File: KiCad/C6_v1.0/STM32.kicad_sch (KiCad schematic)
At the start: 25 parts, among them J1 Conn_01x06_Pin, J2 Conn_01x06_Pin, U1 STM32H562RITx, U2 STM32H7A3RITx, U7 MAX3490xSA

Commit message: commit gng gng
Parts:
- added C32, C33: 2.2u, Capacitor_SMD:C_0805_2012Metric, symbol Device:C
- added J8, J9: Conn_01x02, symbol Connector_Generic:Conn_01x02
- added R49, R50: 10k, Resistor_SMD:R_0805_2012Metric, symbol Device:R
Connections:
- net 3V3: now also J8.1 (Pin_1), J9.1 (Pin_1)
- net GND: now also C32.2, C33.2, R49.2, R50.2
- net at U2.30 (VCAP): now also U2.46 (VCAP), C33.1
- net at U2.60 (BOOT0): now also J8.2 (Pin_2), R49.1
- net EGSE_TX: now reaches U1.16 (PA2)
- net EGSE_RX: now reaches U1.17 (PA3)
- net at U1.30 (VCAP): now also U1.62 (VCAP), C32.1
- net at U1.60 (BOOT0): now also J9.2 (Pin_2), R50.1

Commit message: made voltage sense more accurate to 1%
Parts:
- removed C3: 0.1u, Capacitor_SMD:C_0805_2012Metric, symbol Device:C
- removed FB1: FerriteBead, symbol Device:FerriteBead
- added U10: REF35330QDBVR, Package_TO_SOT_SMD:SOT-23-6, symbol Reference_Voltage:REF35330QDBVR
- C2: value 10u -> 1u
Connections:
- net 3V3: no longer C2.2
- net GND: now also U10.1 (GND), U10.2 (GND)
- net 3V3_REF: now reaches U1.13 (VDDA)
- net 3V3_REF: now also U10.6 (VREF)
- net Vsns: now reaches U1.26 (PB0)
- net I_SCL: now reaches U1.58 (PB6)
- net I_SDA: now reaches U1.59 (PB7)
- new net: C2.2, U10.5 (NR)
- new net 5V: U10.3 (EN), U10.4 (VIN)

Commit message: gooning
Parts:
- J1, J2: footprint (none) -> Connector_PinHeader_2.54mm:PinHeader_1x06_P2.54mm_Vertical

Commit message: gooning
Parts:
- J8, J9: footprint (none) -> Connector_PinHeader_2.54mm:PinHeader_1x02_P2.54mm_Vertical

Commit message: im scared
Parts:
- FB2: footprint (none) -> Resistor_SMD:R_0805_2012Metric

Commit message: DCMI1-Me0
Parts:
- C1, C2, C32, C33, C4, C5, C6, C9: footprint Capacitor_SMD:C_0805_2012Metric -> Capacitor_SMD:C_0402_1005Metric_Pad0.74x0.62mm_HandSolder
- R10, R11, R12, R13, R14, R15, R16, R23, R24, R49, R50, R8, R9: footprint Resistor_SMD:R_0805_2012Metric -> Resistor_SMD:R_0402_1005Metric_Pad0.72x0.64mm_HandSolder
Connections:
- net HALL_C: now reaches U1.20 (PA4)
- net HALL_B: now reaches U1.22 (PA6)
- net HALL_A: now reaches U1.23 (PA7)
- net ESC_PWM: now reaches U1.27 (PB1)
- net ESC_TLM: now reaches U1.57 (PB5)

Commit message: finaly
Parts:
- removed R10, R11, R12, R13: R22, Resistor_SMD:R_0402_1005Metric_Pad0.72x0.64mm_HandSolder, symbol Device:R
- removed R23: 10k, Resistor_SMD:R_0402_1005Metric_Pad0.72x0.64mm_HandSolder, symbol Device:R
- added C10, C3: 2.2u, Capacitor_SMD:C_0402_1005Metric_Pad0.74x0.62mm_HandSolder, symbol Device:C
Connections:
- net SPI_MISO* is gone; now on net SPI_MISO: U1.35 (PB14)
- net SPI_MOSI* is gone; now on net SPI_MOSI: U1.36 (PB15)
- net SPI_NSS* is gone; now on net SPI_NSS: U1.33 (PB12)
- net SPI_SCK* is gone; now on net SPI_SCK: U1.29 (PB10)
- net GND: now also C10.2, C3.2
- net at C32.1, U1.62 (VCAP): no longer U1.30 (VCAP)
- net at C33.1, U2.46 (VCAP): no longer U2.30 (VCAP)
- net DCD_PWDN: no longer names the net of U2.27 (PB1)
- net SPLIT_OE: no longer names the net of U2.10 (PC2)
- new net: C3.1, U2.30 (VCAP)
- new net: C10.1, U1.30 (VCAP)
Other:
- note removed: "Place close to transmit pin"
- note removed: "Source Termination Resistors"

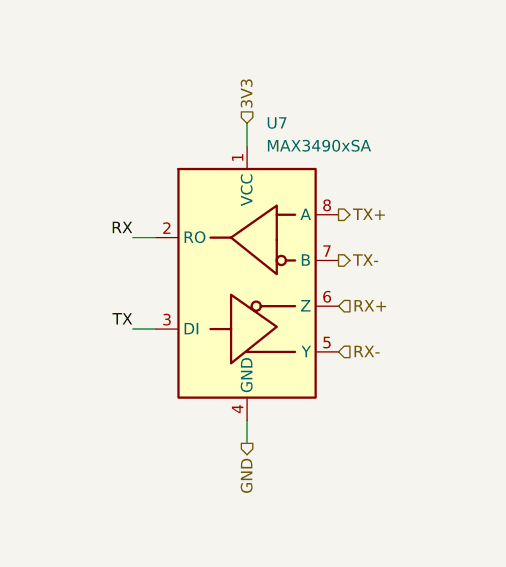
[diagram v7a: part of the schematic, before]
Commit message: made RS-422 120 impedance
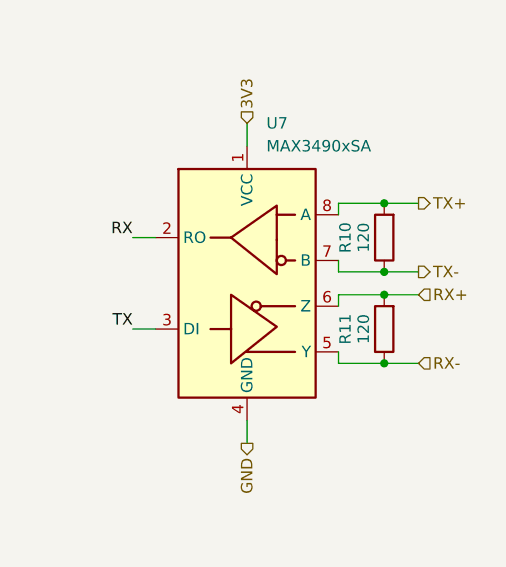
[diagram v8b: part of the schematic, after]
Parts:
- added R10, R11: 120, Resistor_SMD:R_0402_1005Metric_Pad0.72x0.64mm_HandSolder, symbol Device:R
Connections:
- net RX+: now also R11.2
- net RX-: now also R11.1
- net TX+: now also R10.2
- net TX-: now also R10.1
